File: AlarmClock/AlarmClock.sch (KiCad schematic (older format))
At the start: 53 parts

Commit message: Annotate schematics, assign footprints, pcbnew
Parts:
- removed C?: 22p, symbol Device:C
- added C11: 22p, Capacitor_SMD:C_1206_3216Metric_Pad1.33x1.80mm_HandSolder, symbol Device:C
- BT1: renamed from BT?; footprint (none) -> ondra:BatteryHolder_DS1092-04-B6P; Holder type (none) -> DS1092-04-B6P; TME (none) -> https://www.tme.eu/cz/details/ds1092-04-b6p/baterie-pouzdra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
- BZ1: renamed from BZ?; footprint (none) -> Buzzer_Beeper:Buzzer_12x9.5RM7.6
- C1, C2, C3, C5, C6, C7, C9: renamed from C?; footprint (none) -> Capacitor_SMD:C_1206_3216Metric_Pad1.33x1.80mm_HandSolder
- C10: renamed from C?; footprint (none) -> Capacitor_SMD:C_1206_3216Metric_Pad1.33x1.80mm_HandSolder; TME (none) -> https://www.tme.eu/cz/details/vj1206a220jxacw1bc/kondenzato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; TME Symbol (none) -> VJ1206A220JXACW1BC
- C4: renamed from C?; value 100u -> 100u / 16V; footprint (none) -> Capacitor_SMD:CP_Elec_6.3x5.4; GES (none) -> GES05413805
- C8: renamed from C?; value 22u -> 22u / 35V; footprint (none) -> Capacitor_THT:CP_Radial_D5.0mm_P2.00mm; GES (none) -> GES05414160
- J1: renamed from J?; value Barrel_Jack_Switch -> PC-GK2.1; footprint (none) -> Connector_BarrelJack:BarrelJack_Horizontal; TME (none) -> https://www.tme.eu/cz/details/pc-gk2.1/konektory-dc/ninigi/
- J2, J5: renamed from J?; footprint (none) -> Connector_Molex:Molex_KK-254_AE-6410-04A_1x04_P2.54mm_Vertical
- J3: renamed from J?; footprint (none) -> Connector_Molex:Molex_KK-254_AE-6410-02A_1x02_P2.54mm_Vertical
- J4: renamed from J?; footprint (none) -> Connector_IDC:IDC-Header_2x03_P2.54mm_Vertical
- J6, J7: renamed from J?; footprint (none) -> Connector_Molex:Molex_KK-254_AE-6410-03A_1x03_P2.54mm_Vertical
- JP1: renamed from JP?; footprint (none) -> Jumper:SolderJumper-2_P1.3mm_Bridged_Pad1.0x1.5mm
- R1, R10, R11, R12, R13, R14, R15, R16, R2, R3, R4, R5, R6, R7, R8, R9: renamed from R?; footprint (none) -> Resistor_SMD:R_1206_3216Metric_Pad1.30x1.75mm_HandSolder
- SW1, SW2: renamed from SW?; footprint (none) -> Connector_Molex:Molex_KK-254_AE-6410-02A_1x02_P2.54mm_Vertical
- SW3: renamed from SW?; footprint (none) -> Connector_Molex:Molex_KK-254_AE-6410-05A_1x05_P2.54mm_Vertical
- SW4: renamed from SW?; footprint (none) -> Button_Switch_THT:SW_PUSH_6mm_H4.3mm
- Y1: renamed from Y?; footprint (none) -> Crystal:Crystal_HC49-U_Vertical; Part Number TODO 16M-49SMD-SR || 16M-49S-SR -> 16M-49SMD-SR; TME (none) -> https://www.tme.eu/cz/details/16m-49s-sr/krystalove-rezonat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
- gave numbers to parts that had none: 11
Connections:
- net GND: now also C11.2
- net at U2.10 (XTAL2/PB7), Y1.2: now also C11.1
- no-connect marks 0 -> 7
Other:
- note added: "PWM & POWER SWITCHES"
- note added: "Reverse leakage current of D1 amplified by Q2\nwas 1uA with THT 1N4148\nand 2uA with SMD 1N4148."
- note removed: "Reverse leakage current of D? amplified by T?\nwas 1uA with THT 1N4148\nand 2uA with SMD 1N4148."
- moved on the sheet: C4, C5, C6, C8, D2, Q3, R10, R11, R12

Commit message: Design the PCB
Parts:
- added C1: 10n, Capacitor_SMD:C_1206_3216Metric_Pad1.33x1.80mm_HandSolder, symbol Device:C
- added D9: 1N4007, Diode_SMD:D_SMA_Handsoldering, symbol Diode:1N4007
- added JP4, JP5, JP6, JP7: 0 ohm, Resistor_SMD:R_1206_3216Metric_Pad1.30x1.75mm_HandSolder, symbol Jumper:Jumper_2_Bridged
- added R24, R25, R26: 10k, Resistor_SMD:R_1206_3216Metric_Pad1.30x1.75mm_HandSolder, symbol Device:R
- C2: value 100n -> 10n; TME (none) -> https://www.tme.eu/cz/details/c1206c103jaractu/kondenzatory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
- C5: value 100n -> 470n
- C7: value 470n -> 100n
- D3, D4: footprint Diode_THT:D_DO-41_SOD81_P10.16mm_Horizontal -> Diode_SMD:D_SMA_Handsoldering
- SW3: footprint Connector_Molex:Molex_KK-254_AE-6410-05A_1x05_P2.54mm_Vertical -> ondra:Rotary_Encode_Switch_Molex_KK-254_AE-6410-05A_1x05_P2.54mm_Vertical; TME (none) -> https://www.tme.eu/cz/details/pec11r-4220k-s0024/inkrementa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
- renumbered C1 to C17
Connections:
- net +5V: now also D9.1 (K), JP7.1 (A), JP7.2 (B)
- net BTN_snooze: no longer C2.1
- net BTN_stop: no longer C17.1
- net GND: now also C1.2, D9.2 (A), JP6.1 (A); no longer J2.3 (Pin_3)
- net MOSI: now also JP5.2 (B); no longer J4.4 (MOSI)
- net SCL: now also JP4.1 (A); no longer U1.16 (SCL)
- net enc_clk: now also C2.1, R25.2; no longer R7.2, SW3.B
- net enc_dt: now also C1.1, R24.2; no longer R8.2, SW3.A
- net enc_sw: now also C17.1, R26.1; no longer R9.2, SW3.S1
- new net: R24.1, R8.2, SW3.A
- new net: R25.1, R7.2, SW3.B
- new net: R26.2, R9.2, SW3.S1
- new net: J2.3 (Pin_3), JP6.2 (B)
- new net: JP4.2 (B), U1.16 (SCL)
- new net: J4.4 (MOSI), JP5.1 (A)
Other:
- note added: "BZ1 should NOT be abused as a regular buzzer\nbecause that would discharge the battery."
- note added: "POWER LOSS INDICATION"
- note added: "Reverse leakage current of D1 amplified by Q2\nwas 1uA with THT 1N4148 and 2uA with SMD 1N4148."
- note removed: "POWER LOSS INDICATION & BUZZER"
- note removed: "Reverse leakage current of D1 amplified by Q2\nwas 1uA with THT 1N4148\nand 2uA with SMD 1N4148."
- moved on the sheet: C10, C11, C17, C3, C4, C5, C6, C7, C9, J2, J4, R1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

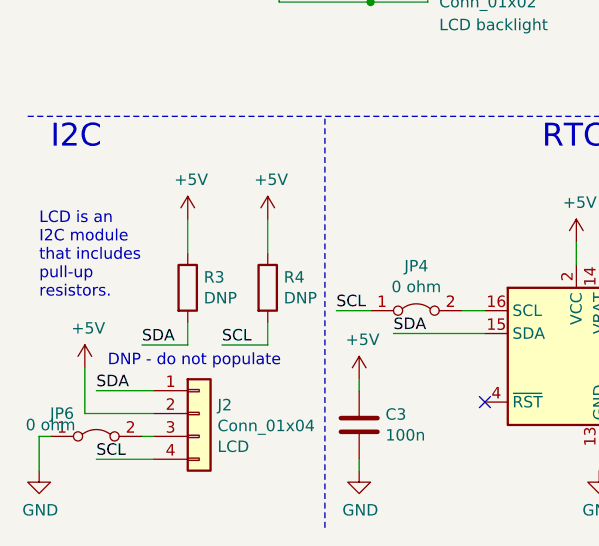
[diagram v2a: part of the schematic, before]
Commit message: Populate I2C pull-up resistors
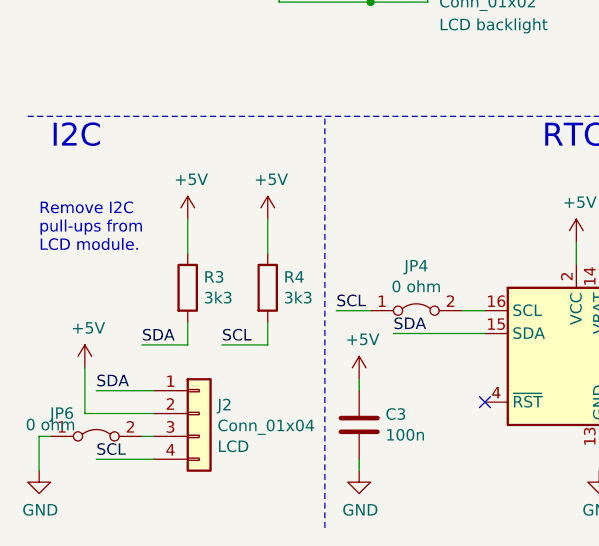
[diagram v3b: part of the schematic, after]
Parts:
- R3, R4: value DNP -> 3k3
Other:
- note added: "Remove I2C\npull-ups from\nLCD module."
- note removed: "DNP - do not populate"
- note removed: "LCD is an\nI2C module\nthat includes\npull-up\nresistors."
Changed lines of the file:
@@
 Wire Wire Line
 	10550 1100 10650 1100
-Text Notes 550  6800 0    50   ~ 0
-LCD is an\nI2C module\nthat includes\npull-up\nresistors.
+Text Notes 550  6600 0    50   ~ 0
+Remove I2C\npull-ups from\nLCD module.
 $Comp
 L Device:R R3
@@
 P 1200 6750
 F 0 "R3" H 1270 6796 50  0000 L CNN
-F 1 "DNP" H 1270 6705 50  0000 L CNN
+F 1 "3k3" H 1270 6705 50  0000 L CNN
 F 2 "Resistor_SMD:R_1206_3216Metric_Pad1.30x1.75mm_HandSolder" V 1130 6750 50  0001 C CNN
 F 3 "~" H 1200 6750 50  0001 C CNN
 	1    1200 6750
-	1    0    0    -1
-$EndComp
-$Comp
-L Device:R R4
-U 1 1 624B2FD2
-P 1550 6750
-F 0 "R4" H 1620 6796 50  0000 L CNN
-F 1 "DNP" H 1620 6705 50  0000 L CNN
-F 2 "Resistor_SMD:R_1206_3216Metric_Pad1.30x1.75mm_HandSolder" V 1480 6750 50  0001 C CNN
-F 3 "~" H 1550 6750 50  0001 C CNN
-	1    1550 6750
 	1    0    0    -1
 $EndComp
@@
 Text Notes 1600 650  0    100  ~ 0
 BUTTONS & CONTROLS
-Text Notes 850  7100 0    50   ~ 0
-DNP - do not populate
 Wire Notes Line
 	500  6000 6950 6000
@@
 Wire Wire Line
 	1550 3800 1550 3900
+$Comp
+L Device:R R4
+U 1 1 624B2FD2
+P 1550 6750
+F 0 "R4" H 1620 6796 50  0000 L CNN
+F 1 "3k3" H 1620 6705 50  0000 L CNN
+F 2 "Resistor_SMD:R_1206_3216Metric_Pad1.30x1.75mm_HandSolder" V 1480 6750 50  0001 C CNN
+F 3 "~" H 1550 6750 50  0001 C CNN
+	1    1550 6750
+	1    0    0    -1
+$EndComp
 $EndSCHEMATC

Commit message: Fix ambient LED staying lit
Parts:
- SW4: TME (none) -> https://www.tme.eu/cz/details/skhhama010/mikrospinace-tact/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
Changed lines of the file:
@@
 F 1 "SW_Push" V 8095 4998 50  0000 L CNN
 F 2 "Button_Switch_THT:SW_PUSH_6mm_H4.3mm" H 8050 5050 50  0001 C CNN
-F 3 "~" H 8050 5050 50  0001 C CNN
+F 3 "https://www.tme.eu/Document/49afa6e9f9d0b38495230e99c7b0948e/SKHHAMA010.PDF" H 8050 5050 50  0001 C CNN
 F 4 "RESET" V 8200 5100 50  0000 C CNN "Label"
+F 5 "https://www.tme.eu/cz/details/skhhama010/mikrospinace-tact/alps/" V 8050 4850 50  0001 C CNN "TME"
 	1    8050 4850
 	0    1    1    0

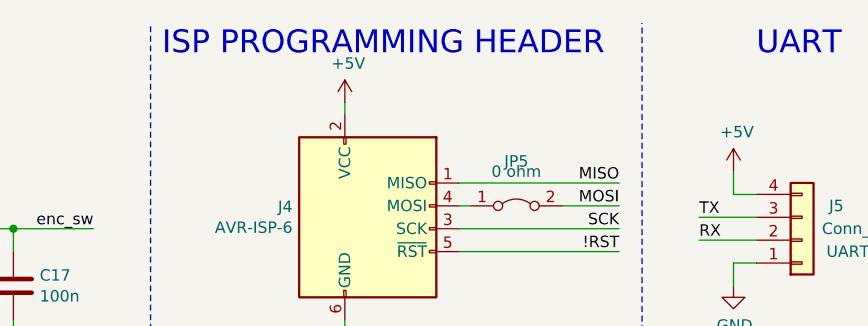
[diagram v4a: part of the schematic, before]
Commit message: Update text in AlarmClock schematic
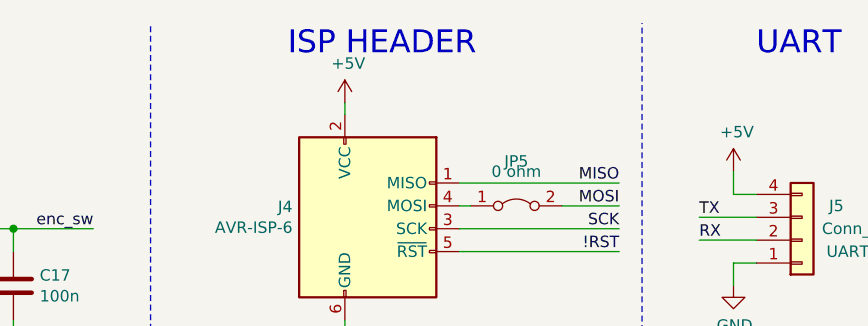
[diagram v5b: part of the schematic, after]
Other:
- note added: "ISP HEADER"
- note removed: "ISP PROGRAMMING HEADER"
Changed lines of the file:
@@
 Wire Notes Line
 	7250 2100 7250 500
-Text Notes 5150 650  0    100  ~ 0
-ISP PROGRAMMING HEADER
 Wire Wire Line
 	5950 850  5950 900
@@
 	1    0    0    -1
 $EndComp
+Text Notes 5700 650  0    100  ~ 0
+ISP HEADER
 $EndSCHEMATC

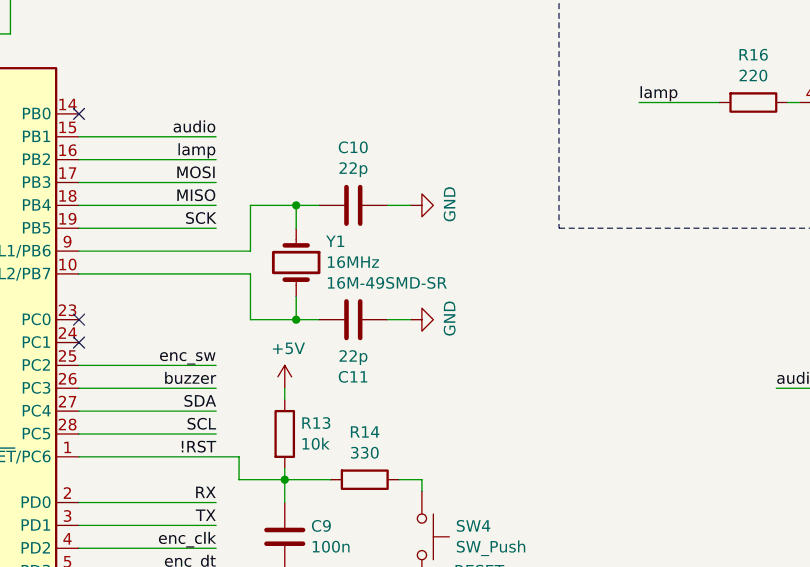
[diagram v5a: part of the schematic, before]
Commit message: Update symbol fields for BOM
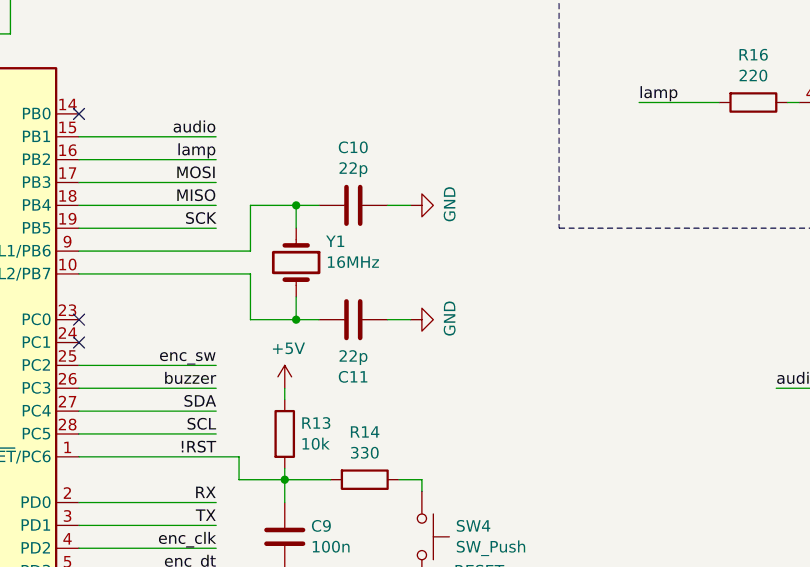
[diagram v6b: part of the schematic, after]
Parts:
- C1, C2: TME Symbol (none) -> C1206C103JARACTU
- C17, C3, C7, C9: GES (none) -> GES05400125
- C5: GES (none) -> GES13004463
- J1: TME Symbol (none) -> PC-GK2.1
- Q4, Q5: TME (none) -> https://www.tme.eu/cz/details/irl6342trpbf/tranzistory-s-ka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; TME Symbol (none) -> IRL6342TRPBF
- SW3: TME Symbol (none) -> PEC11R-4220K-S0024
- SW4: TME Symbol (none) -> SKHHAMA010
- Y1: Part Number 16M-49SMD-SR -> (none); TME Symbol (none) -> 16M-49SMD-SR
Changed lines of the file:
@@
 F 2 "Capacitor_SMD:C_1206_3216Metric_Pad1.33x1.80mm_HandSolder" H 4538 1500 50  0001 C CNN
 F 3 "~" H 4500 1650 50  0001 C CNN
+F 4 "GES05400125" H 4500 1650 50  0001 C CNN "GES"
 	1    4500 1650
 	1    0    0    -1
@@
 F 2 "Capacitor_SMD:C_1206_3216Metric_Pad1.33x1.80mm_HandSolder" H 5138 4350 50  0001 C CNN
 F 3 "~" H 5100 4500 50  0001 C CNN
+F 4 "GES05400125" H 5100 4500 50  0001 C CNN "GES"
 	1    5100 4500
 	1    0    0    -1
@@
 F 3 "https://www.tme.eu/Document/8c1b1e629e264c85ef5bd42048515675/PEC11R.pdf" H 3450 1760 50  0001 C CNN
 F 4 "https://www.tme.eu/cz/details/pec11r-4220k-s0024/inkrementalni-enkodery/bourns/" H 3450 1500 50  0001 C CNN "TME"
+F 5 "PEC11R-4220K-S0024" H 3450 1500 50  0001 C CNN "TME Symbol"
 	1    3450 1500
 	1    0    0    -1
@@
 F 2 "Capacitor_SMD:C_1206_3216Metric_Pad1.33x1.80mm_HandSolder" H 1988 7200 50  0001 C CNN
 F 3 "~" H 1950 7350 50  0001 C CNN
+F 4 "GES05400125" H 1950 7350 50  0001 C CNN "GES"
 	1    1950 7350
 	1    0    0    -1
@@
 F 3 "https://www.tme.eu/Document/0c2caa550314868a0a12e8b9344a6069/pc-gk2.1.pdf" H 1100 3960 50  0001 C CNN
 F 4 "https://www.tme.eu/cz/details/pc-gk2.1/konektory-dc/ninigi/" H 1050 4000 50  0001 C CNN "TME"
+F 5 "PC-GK2.1" H 1050 4000 50  0001 C CNN "TME Symbol"
 	1    1050 4000
 	1    0    0    -1
@@
 F 2 "Crystal:Crystal_HC49-U_Vertical" H 7500 3650 50  0001 C CNN
 F 3 "https://www.tme.eu/cz/details/16m-49s-sr/krystalove-rezonatory-tht/sr-passives/" H 7500 3650 50  0001 C CNN
-F 4 "16M-49SMD-SR" V 7591 3781 50  0000 L CNN "Part Number"
-F 5 "https://www.tme.eu/cz/details/16m-49s-sr/krystalove-rezonatory-tht/sr-passives/" V 7500 3650 50  0001 C CNN "TME"
+F 4 "https://www.tme.eu/cz/details/16m-49s-sr/krystalove-rezonatory-tht/sr-passives/" V 7500 3650 50  0001 C CNN "TME"
+F 5 "16M-49SMD-SR" V 7500 3650 50  0001 C CNN "TME Symbol"
 	1    7500 3650
 	0    1    1    0
@@
 F 2 "Package_SO:SOIC-8_3.9x4.9mm_P1.27mm" H 10100 2850 50  0001 L CNN
 F 3 "https://www.infineon.com/dgdl/irl6342pbf.pdf?fileId=5546d462533600a40153565ffb7a2577" H 9900 2950 50  0001 L CNN
+F 4 "https://www.tme.eu/cz/details/irl6342trpbf/tranzistory-s-kanalem-n-smd/infineon-technologies/" H 9900 2950 50  0001 C CNN "TME"
+F 5 "IRL6342TRPBF" H 9900 2950 50  0001 C CNN "TME Symbol"
 	1    9900 2950
 	1    0    0    -1
@@
 F 2 "Package_SO:SOIC-8_3.9x4.9mm_P1.27mm" H 10100 1400 50  0001 L CNN
 F 3 "https://www.infineon.com/dgdl/irl6342pbf.pdf?fileId=5546d462533600a40153565ffb7a2577" H 9900 1500 50  0001 L CNN
+F 4 "https://www.tme.eu/cz/details/irl6342trpbf/tranzistory-s-kanalem-n-smd/infineon-technologies/" H 9900 1500 50  0001 C CNN "TME"
+F 5 "IRL6342TRPBF" H 9900 1500 50  0001 C CNN "TME Symbol"
 	1    9900 1500
 	1    0    0    -1
@@
 F 2 "Capacitor_SMD:C_1206_3216Metric_Pad1.33x1.80mm_HandSolder" H 7488 4700 50  0001 C CNN
 F 3 "~" H 7450 4850 50  0001 C CNN
+F 4 "GES05400125" H 7450 4850 50  0001 C CNN "GES"
 	1    7450 4850
 	1    0    0    -1
@@
 F 4 "RESET" V 8200 5100 50  0000 C CNN "Label"
 F 5 "https://www.tme.eu/cz/details/skhhama010/mikrospinace-tact/alps/" V 8050 4850 50  0001 C CNN "TME"
+F 6 "SKHHAMA010" H 8050 4850 50  0001 C CNN "TME Symbol"
 	1    8050 4850
 	0    1    1    0
@@
 F 1 "AVR-ISP-6" H 5721 1405 50  0000 R CNN
 F 2 "Connector_IDC:IDC-Header_2x03_P2.54mm_Vertical" V 5800 1450 50  0001 C CNN
-F 3 " ~" H 4775 850 50  0001 C CNN
+F 3 "~" H 4775 850 50  0001 C CNN
 	1    6050 1400
 	1    0    0    -1
@@
 F 2 "Capacitor_SMD:C_1206_3216Metric_Pad1.33x1.80mm_HandSolder" H 3788 3850 50  0001 C CNN
 F 3 "~" H 3750 4000 50  0001 C CNN
+F 4 "GES13004463" H 3750 4000 50  0001 C CNN "GES"
 	1    3750 4000
 	1    0    0    -1
@@
 F 3 "https://www.tme.eu/Document/653c0d3264f3d0a9a137261f4ec67d5d/KEM_C1011_X7R_TIP_RING_SMD.pdf" H 2050 1850 50  0001 C CNN
 F 4 "https://www.tme.eu/cz/details/c1206c103jaractu/kondenzatory-mlcc-smd-1206/kemet/" H 2050 1850 50  0001 C CNN "TME"
+F 5 "C1206C103JARACTU" H 2050 1850 50  0001 C CNN "TME Symbol"
 	1    2050 1850
 	1    0    0    -1
@@
 F 3 "https://www.tme.eu/Document/653c0d3264f3d0a9a137261f4ec67d5d/KEM_C1011_X7R_TIP_RING_SMD.pdf" H 2400 1850 50  0001 C CNN
 F 4 "https://www.tme.eu/cz/details/c1206c103jaractu/kondenzatory-mlcc-smd-1206/kemet/" H 2400 1850 50  0001 C CNN "TME"
+F 5 "C1206C103JARACTU" H 2400 1850 50  0001 C CNN "TME Symbol"
 	1    2400 1850
 	1    0    0    -1
